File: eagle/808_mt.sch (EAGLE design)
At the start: 59 parts, among them IC1 TL071P, IC2 TL072P, Q1 2N3904, Q2 2N3906, Q3 2N3904, SW8 808_LT_MSS42_SW_4PDT

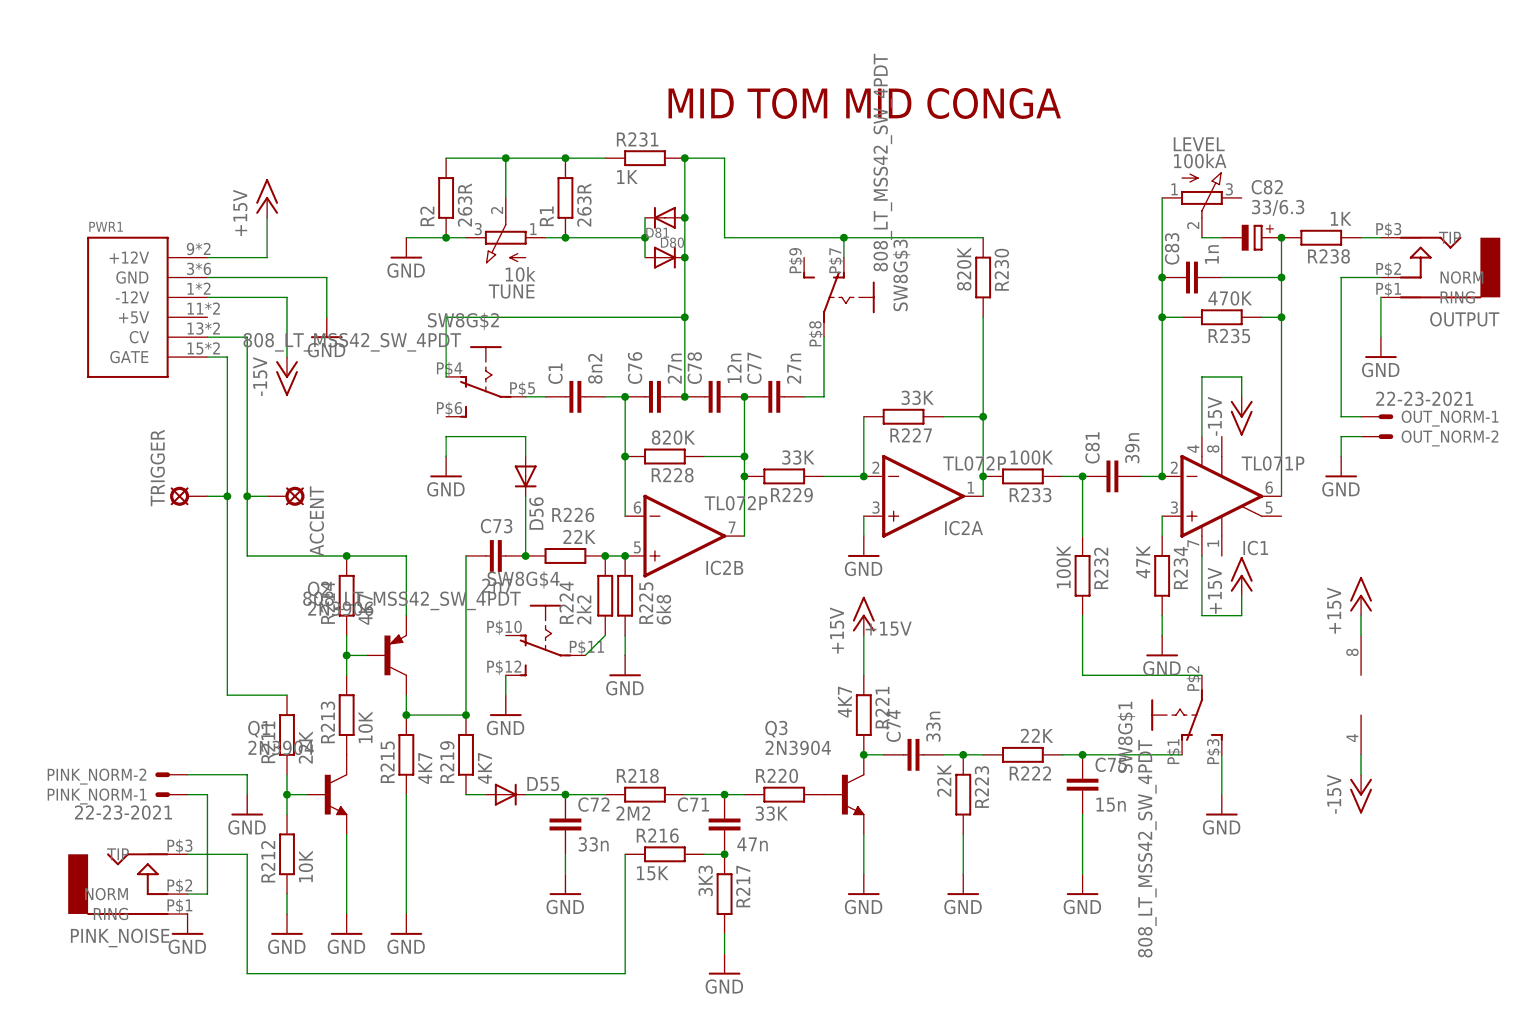
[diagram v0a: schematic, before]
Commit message: changed values for hitom
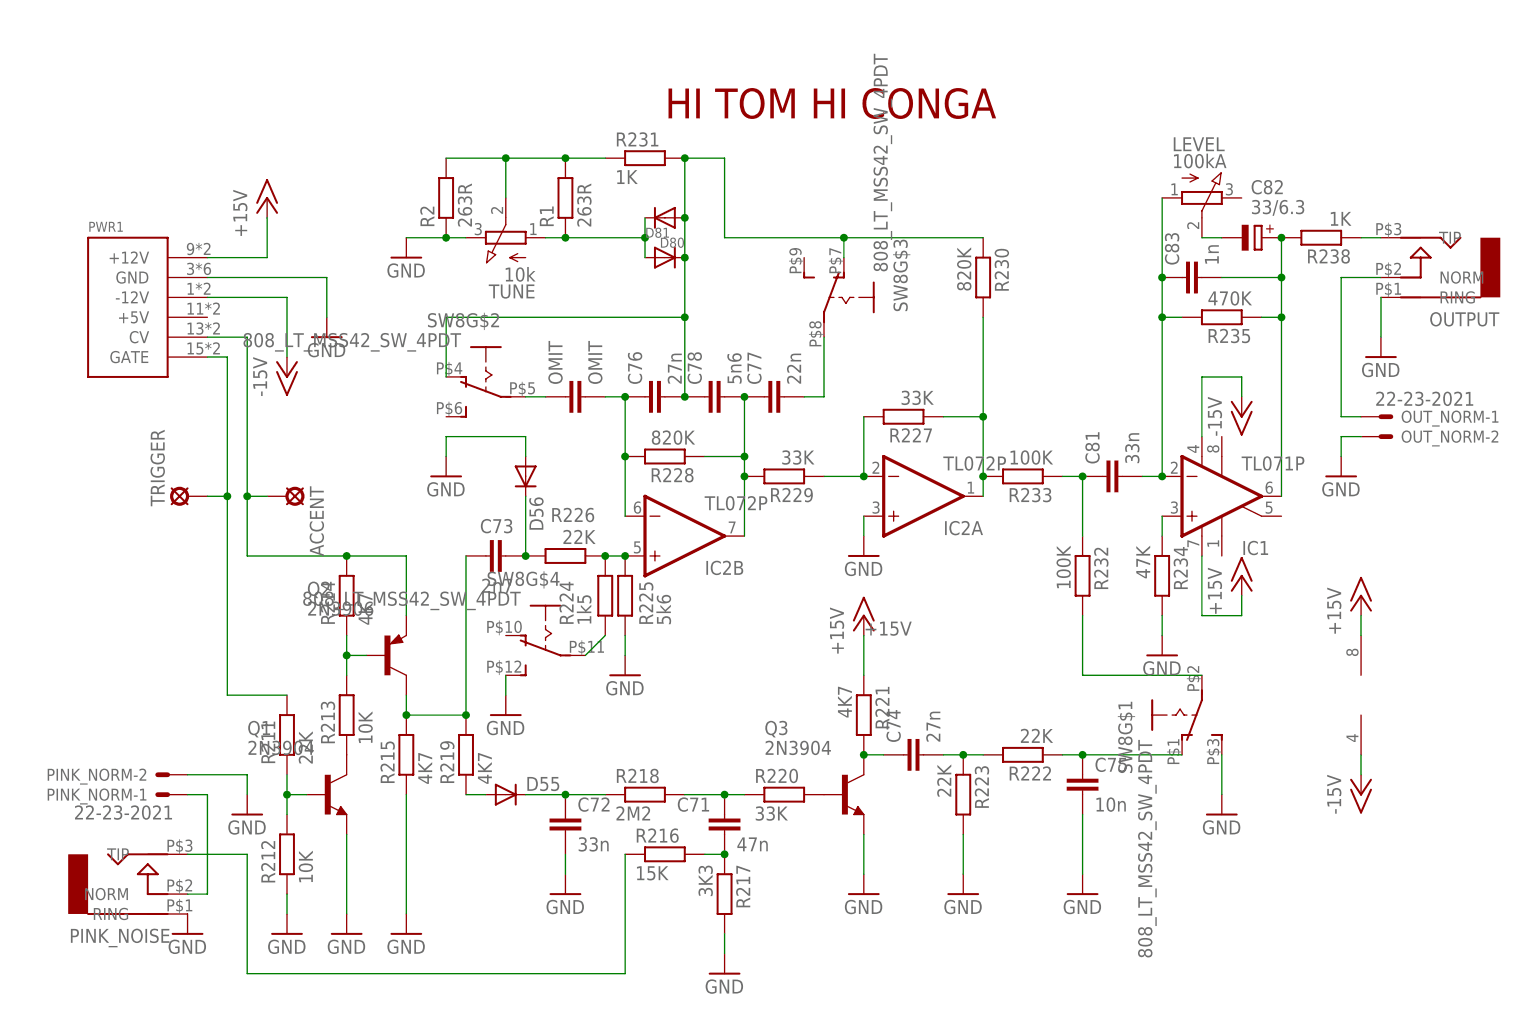
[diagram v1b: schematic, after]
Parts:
- C74: value 33n -> 27n
- C75: value 15n -> 10n
- C77: value 27n -> 22n
- C78: value 12n -> 5n6
- C81: value 39n -> 33n
- OMIT: value 8n2 -> OMIT
- R224: value 2k2 -> 1k5
- R225: value 6k8 -> 5k6
- renumbered C1 to OMIT
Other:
- note added: "HI TOM HI CONGA"
- note removed: "MID TOM MID CONGA"
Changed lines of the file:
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@@
 <?xml version="1.0" encoding="utf-8"?>
 <!DOCTYPE eagle SYSTEM "eagle.dtd">
-<eagle version="7.1.0">
+<eagle version="7.2.0">
 <drawing>
 <settings>
@@
 <part name="R219" library="TR808clone" deviceset="R-EU_" device="0207/7" value="4K7"/>
 <part name="C73" library="TR808clone" deviceset="C-EU" device="4MM_PITCH" value="2n7"/>
-<part name="R225" library="TR808clone" deviceset="R-EU_" device="0207/7" value="6k8"/>
+<part name="R225" library="TR808clone" deviceset="R-EU_" device="0207/7" value="5k6"/>
 <part name="V147" library="supply1" deviceset="GND" device=""/>
 <part name="R228" library="TR808clone" deviceset="R-EU_" device="0207/7" value="820K"/>
 <part name="C76" library="TR808clone" deviceset="C-EU" device="050-024X044" value="27n"/>
-<part name="C78" library="TR808clone" deviceset="C-EU" device="3.5MM_PITCH" value="12n"/>
-<part name="C77" library="TR808clone" deviceset="C-EU" device="050-024X044" value="27n"/>
+<part name="C78" library="TR808clone" deviceset="C-EU" device="3.5MM_PITCH" value="5n6"/>
+<part name="C77" library="TR808clone" deviceset="C-EU" device="050-024X044" value="22n"/>
 <part name="R229" library="TR808clone" deviceset="R-EU_" device="0207/7" value="33K"/>
 <part name="R227" library="TR808clone" deviceset="R-EU_" device="0207/7" value="33K"/>
@@
 <part name="V149" library="supply1" deviceset="GND" device=""/>
 <part name="R233" library="TR808clone" deviceset="R-EU_" device="0207/7" value="100K"/>
-<part name="C81" library="TR808clone" deviceset="C-EU" device="050-024X044" value="39n"/>
+<part name="C81" library="TR808clone" deviceset="C-EU" device="050-024X044" value="33n"/>
 <part name="R234" library="TR808clone" deviceset="R-EU_" device="0207/7" value="47K"/>
 <part name="V150" library="supply1" deviceset="GND" device=""/>
@@
 <part name="C82" library="TR808clone" deviceset="CPOL-EU" device="E2-5" value="33/6.3"/>
 <part name="R238" library="TR808clone" deviceset="R-EU_" device="0207/7" value="1K"/>
-<part name="C75" library="TR808clone" deviceset="C-EU" device="4MM_PITCH" value="15n"/>
+<part name="C75" library="TR808clone" deviceset="C-EU" device="4MM_PITCH" value="10n"/>
 <part name="R223" library="TR808clone" deviceset="R-EU_" device="0207/7" value="22K"/>
-<part name="C74" library="TR808clone" deviceset="C-EU" device="050-024X044" value="33n"/>
+<part name="C74" library="TR808clone" deviceset="C-EU" device="050-024X044" value="27n"/>
 <part name="R221" library="TR808clone" deviceset="R-EU_" device="0207/7" value="4K7"/>
 <part name="V151" library="supply1" deviceset="GND" device=""/>
@@
 <part name="V155" library="supply1" deviceset="GND" device=""/>
 <part name="V156" library="supply1" deviceset="GND" device=""/>
-<part name="R224" library="TR808clone" deviceset="R-EU_" device="0207/7" value="2k2"/>
+<part name="R224" library="TR808clone" deviceset="R-EU_" device="0207/7" value="1k5"/>
 <part name="V159" library="supply1" deviceset="GND" device=""/>
 <part name="V160" library="supply1" deviceset="GND" device=""/>
@@
 <part name="TRIGGER" library="solpad" deviceset="LSP10" device=""/>
 <part name="ACCENT" library="solpad" deviceset="LSP10" device=""/>
-<part name="C1" library="TR808clone" deviceset="C-EU" device="050-024X044" value="8n2"/>
+<part name="OMIT" library="TR808clone" deviceset="C-EU" device="050-024X044" value="OMIT"/>
 </parts>
 <sheets>
 <sheet>
 <plain>
-<text x="50.8" y="96.52" size="3.81" layer="94">MID TOM MID CONGA</text>
+<text x="50.8" y="96.52" size="3.81" layer="94">HI TOM HI CONGA</text>
 </plain>
 <instances>
@@
 <instance part="ACCENT" gate="1" x="2.54" y="48.26" rot="R270"/>
 <instance part="SW8" gate="G$2" x="27.94" y="63.5" rot="MR270"/>
-<instance part="C1" gate="G$1" x="38.1" y="60.96" rot="R90"/>
+<instance part="OMIT" gate="G$1" x="38.1" y="60.96" rot="R90"/>
 </instances>
 <busses>
@@
 <pinref part="C76" gate="G$1" pin="1"/>
 <pinref part="IC2" gate="B" pin="-IN"/>
-<pinref part="C1" gate="G$1" pin="2"/>
+<pinref part="OMIT" gate="G$1" pin="2"/>
 <wire x1="43.18" y1="60.96" x2="45.72" y2="60.96" width="0.1524" layer="91"/>
 <junction x="45.72" y="60.96"/>
@@
 <segment>
 <pinref part="SW8" gate="G$2" pin="P"/>
-<pinref part="C1" gate="G$1" pin="1"/>
+<pinref part="OMIT" gate="G$1" pin="1"/>
 <wire x1="33.02" y1="60.96" x2="35.56" y2="60.96" width="0.1524" layer="91"/>
 </segment>

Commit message: values for low tom
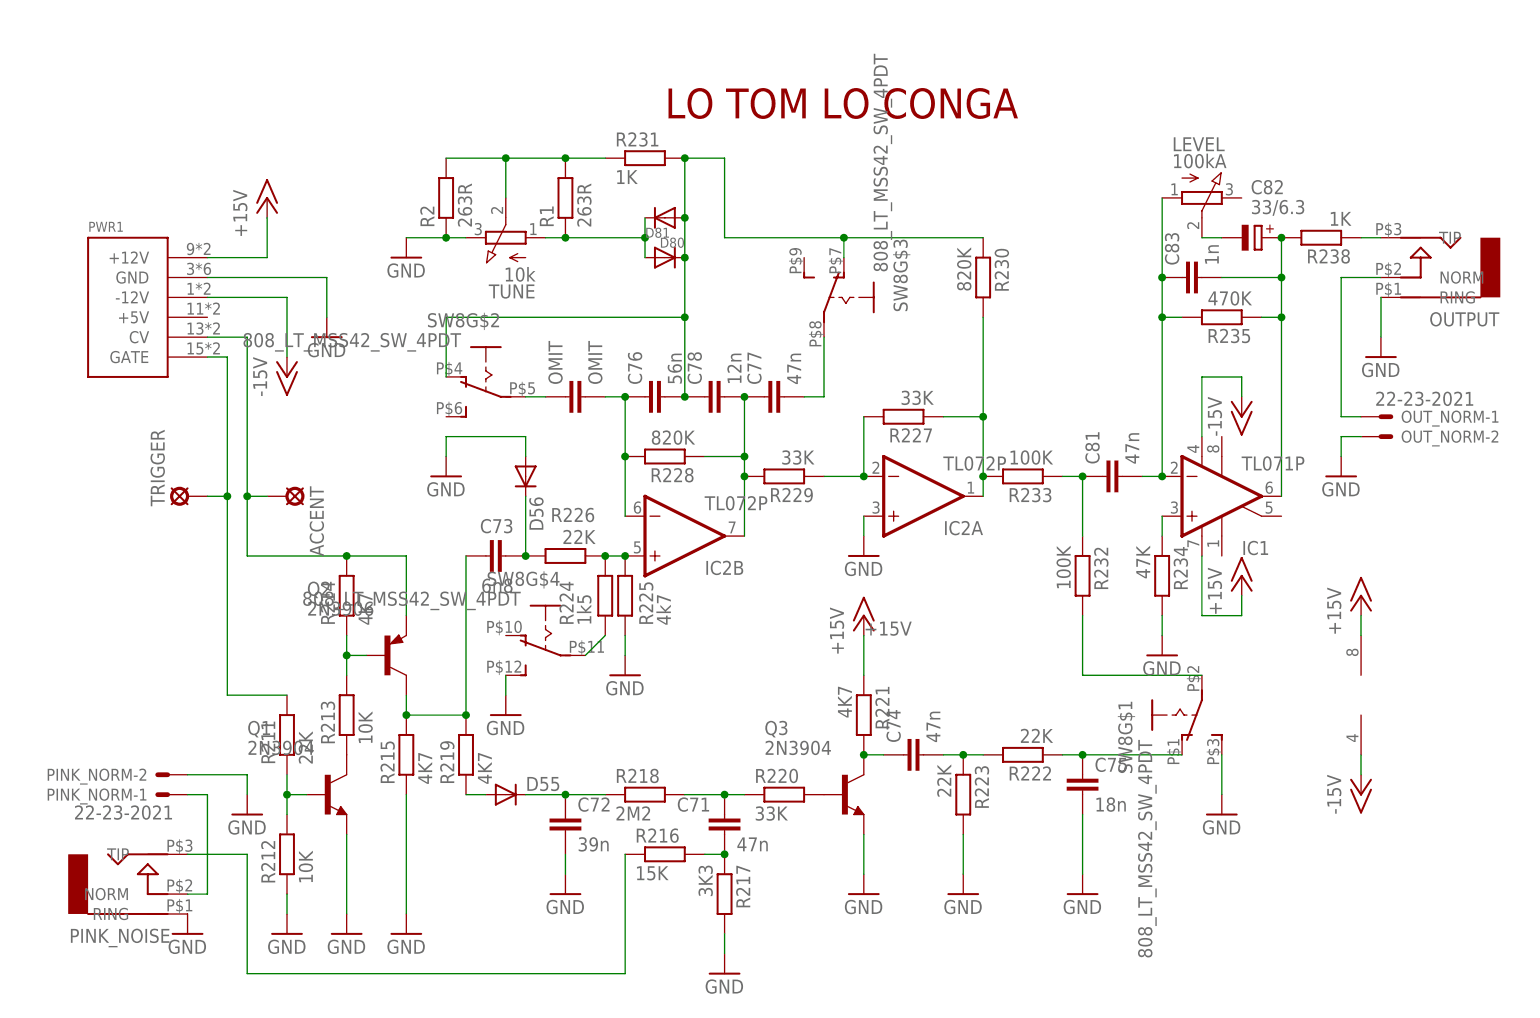
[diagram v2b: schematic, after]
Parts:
- C72: value 33n -> 39n
- C73: value 2n7 -> 6n8
- C74: value 27n -> 47n
- C75: value 10n -> 18n
- C76: value 27n -> 56n
- C77: value 22n -> 47n
- C78: value 5n6 -> 12n
- C81: value 33n -> 47n
- R225: value 5k6 -> 4k7
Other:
- note added: "LO TOM LO CONGA"
- note removed: "HI TOM HI CONGA"
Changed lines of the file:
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@@
 <?xml version="1.0" encoding="utf-8"?>
 <!DOCTYPE eagle SYSTEM "eagle.dtd">
-<eagle version="7.2.0">
+<eagle version="7.1.0">
 <drawing>
 <settings>
@@
 <part name="V145" library="supply1" deviceset="GND" device=""/>
 <part name="R219" library="TR808clone" deviceset="R-EU_" device="0207/7" value="4K7"/>
-<part name="C73" library="TR808clone" deviceset="C-EU" device="4MM_PITCH" value="2n7"/>
-<part name="R225" library="TR808clone" deviceset="R-EU_" device="0207/7" value="5k6"/>
+<part name="C73" library="TR808clone" deviceset="C-EU" device="4MM_PITCH" value="6n8"/>
+<part name="R225" library="TR808clone" deviceset="R-EU_" device="0207/7" value="4k7"/>
 <part name="V147" library="supply1" deviceset="GND" device=""/>
 <part name="R228" library="TR808clone" deviceset="R-EU_" device="0207/7" value="820K"/>
-<part name="C76" library="TR808clone" deviceset="C-EU" device="050-024X044" value="27n"/>
-<part name="C78" library="TR808clone" deviceset="C-EU" device="3.5MM_PITCH" value="5n6"/>
-<part name="C77" library="TR808clone" deviceset="C-EU" device="050-024X044" value="22n"/>
+<part name="C76" library="TR808clone" deviceset="C-EU" device="050-024X044" value="56n"/>
+<part name="C78" library="TR808clone" deviceset="C-EU" device="3.5MM_PITCH" value="12n"/>
+<part name="C77" library="TR808clone" deviceset="C-EU" device="050-024X044" value="47n"/>
 <part name="R229" library="TR808clone" deviceset="R-EU_" device="0207/7" value="33K"/>
 <part name="R227" library="TR808clone" deviceset="R-EU_" device="0207/7" value="33K"/>
@@
 <part name="V149" library="supply1" deviceset="GND" device=""/>
 <part name="R233" library="TR808clone" deviceset="R-EU_" device="0207/7" value="100K"/>
-<part name="C81" library="TR808clone" deviceset="C-EU" device="050-024X044" value="33n"/>
+<part name="C81" library="TR808clone" deviceset="C-EU" device="050-024X044" value="47n"/>
 <part name="R234" library="TR808clone" deviceset="R-EU_" device="0207/7" value="47K"/>
 <part name="V150" library="supply1" deviceset="GND" device=""/>
@@
 <part name="C82" library="TR808clone" deviceset="CPOL-EU" device="E2-5" value="33/6.3"/>
 <part name="R238" library="TR808clone" deviceset="R-EU_" device="0207/7" value="1K"/>
-<part name="C75" library="TR808clone" deviceset="C-EU" device="4MM_PITCH" value="10n"/>
+<part name="C75" library="TR808clone" deviceset="C-EU" device="4MM_PITCH" value="18n"/>
 <part name="R223" library="TR808clone" deviceset="R-EU_" device="0207/7" value="22K"/>
-<part name="C74" library="TR808clone" deviceset="C-EU" device="050-024X044" value="27n"/>
+<part name="C74" library="TR808clone" deviceset="C-EU" device="050-024X044" value="47n"/>
 <part name="R221" library="TR808clone" deviceset="R-EU_" device="0207/7" value="4K7"/>
 <part name="V151" library="supply1" deviceset="GND" device=""/>
@@
 <part name="R218" library="TR808clone" deviceset="R-EU_" device="0207/7" value="2M2"/>
 <part name="D55" library="adafruit" deviceset="DIODE" device="DO-1N4148"/>
-<part name="C72" library="TR808clone" deviceset="C-EU" device="050-024X044" value="33n"/>
+<part name="C72" library="TR808clone" deviceset="C-EU" device="050-024X044" value="39n"/>
 <part name="V155" library="supply1" deviceset="GND" device=""/>
 <part name="V156" library="supply1" deviceset="GND" device=""/>
@@
 <sheet>
 <plain>
-<text x="50.8" y="96.52" size="3.81" layer="94">HI TOM HI CONGA</text>
+<text x="50.8" y="96.52" size="3.81" layer="94">LO TOM LO CONGA</text>
 </plain>
 <instances>
